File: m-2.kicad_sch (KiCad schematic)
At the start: 58 parts, among them J301 1-2199230-6, J302 2199230-6, M1 M2_4222, M301 M2_2280, U301 74LVC2G07GV, U302 74LVC2G07GV

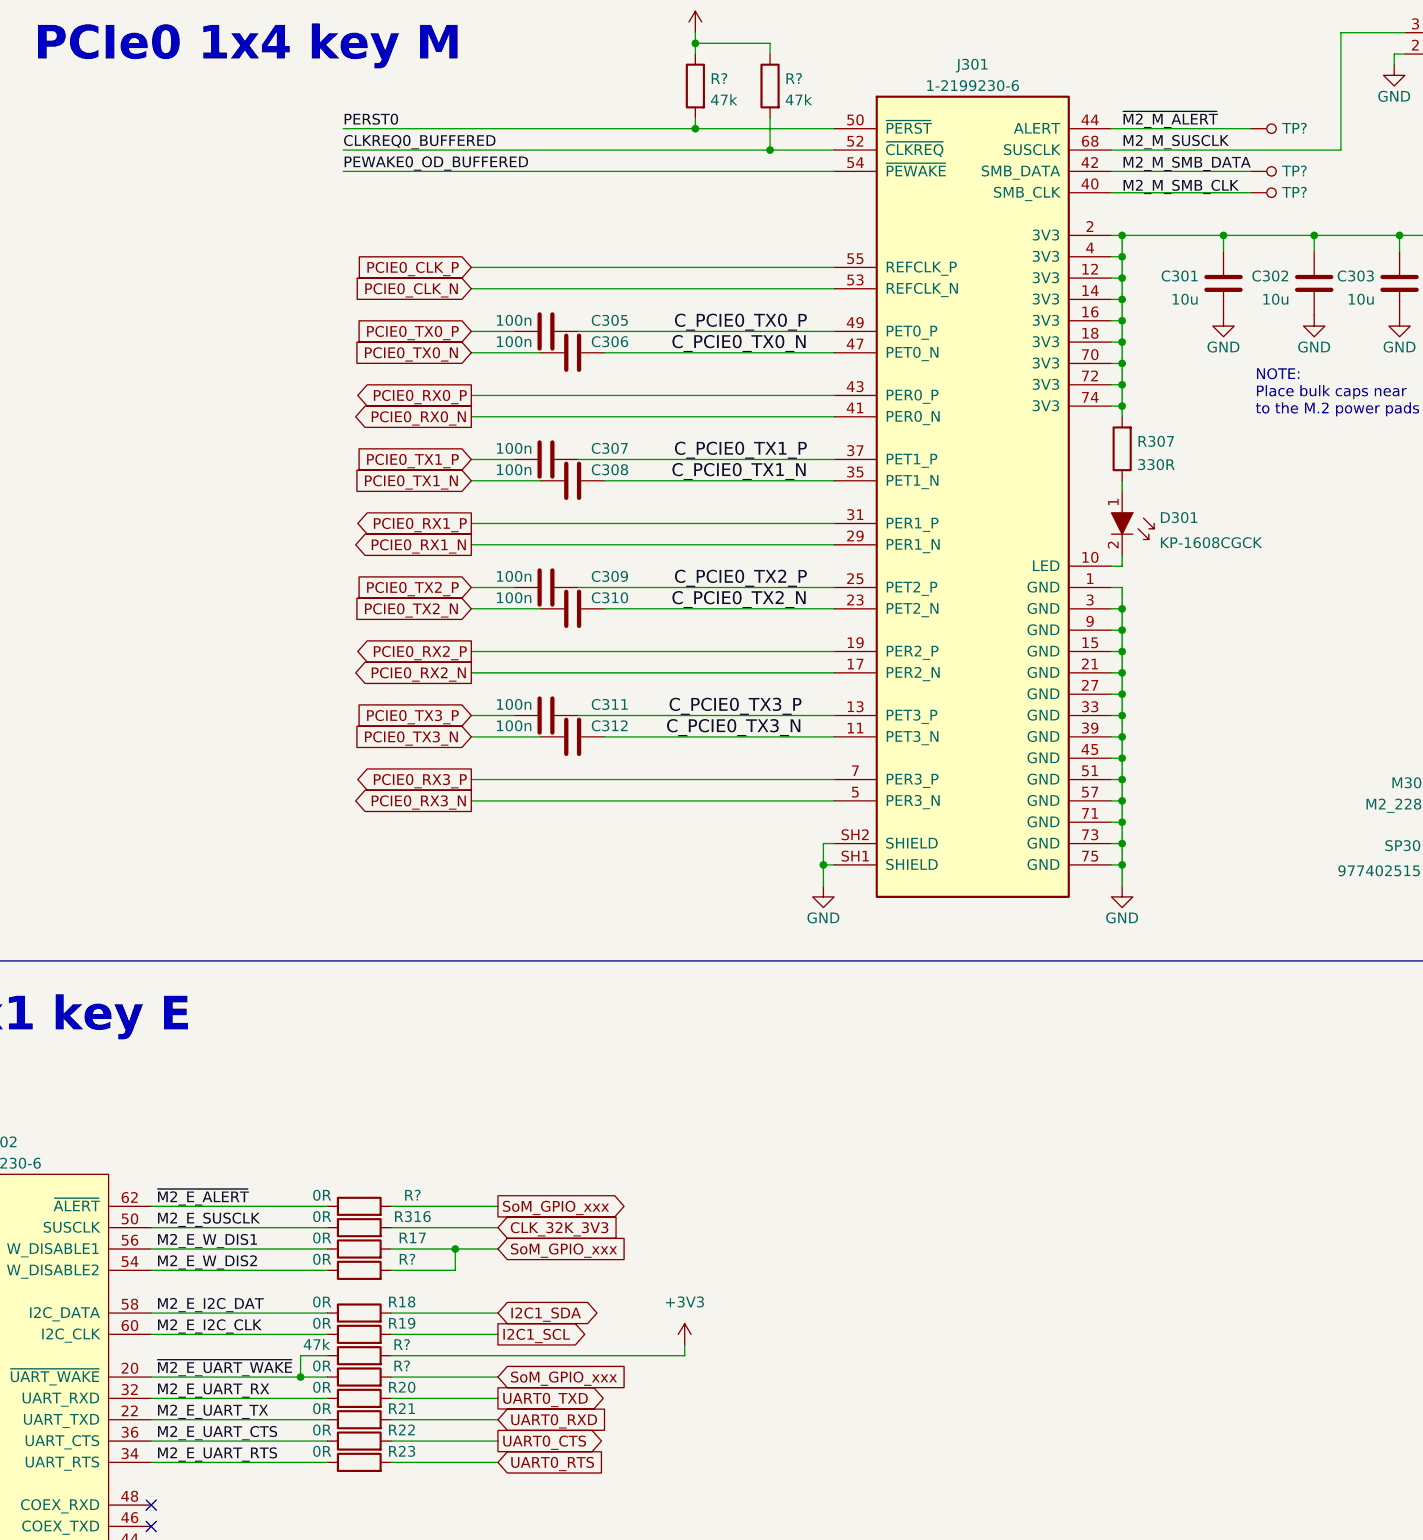
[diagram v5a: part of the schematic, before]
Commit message: Unused M.2 pins as test-point, M2 key E I2C and UART wake resistors set to DNP
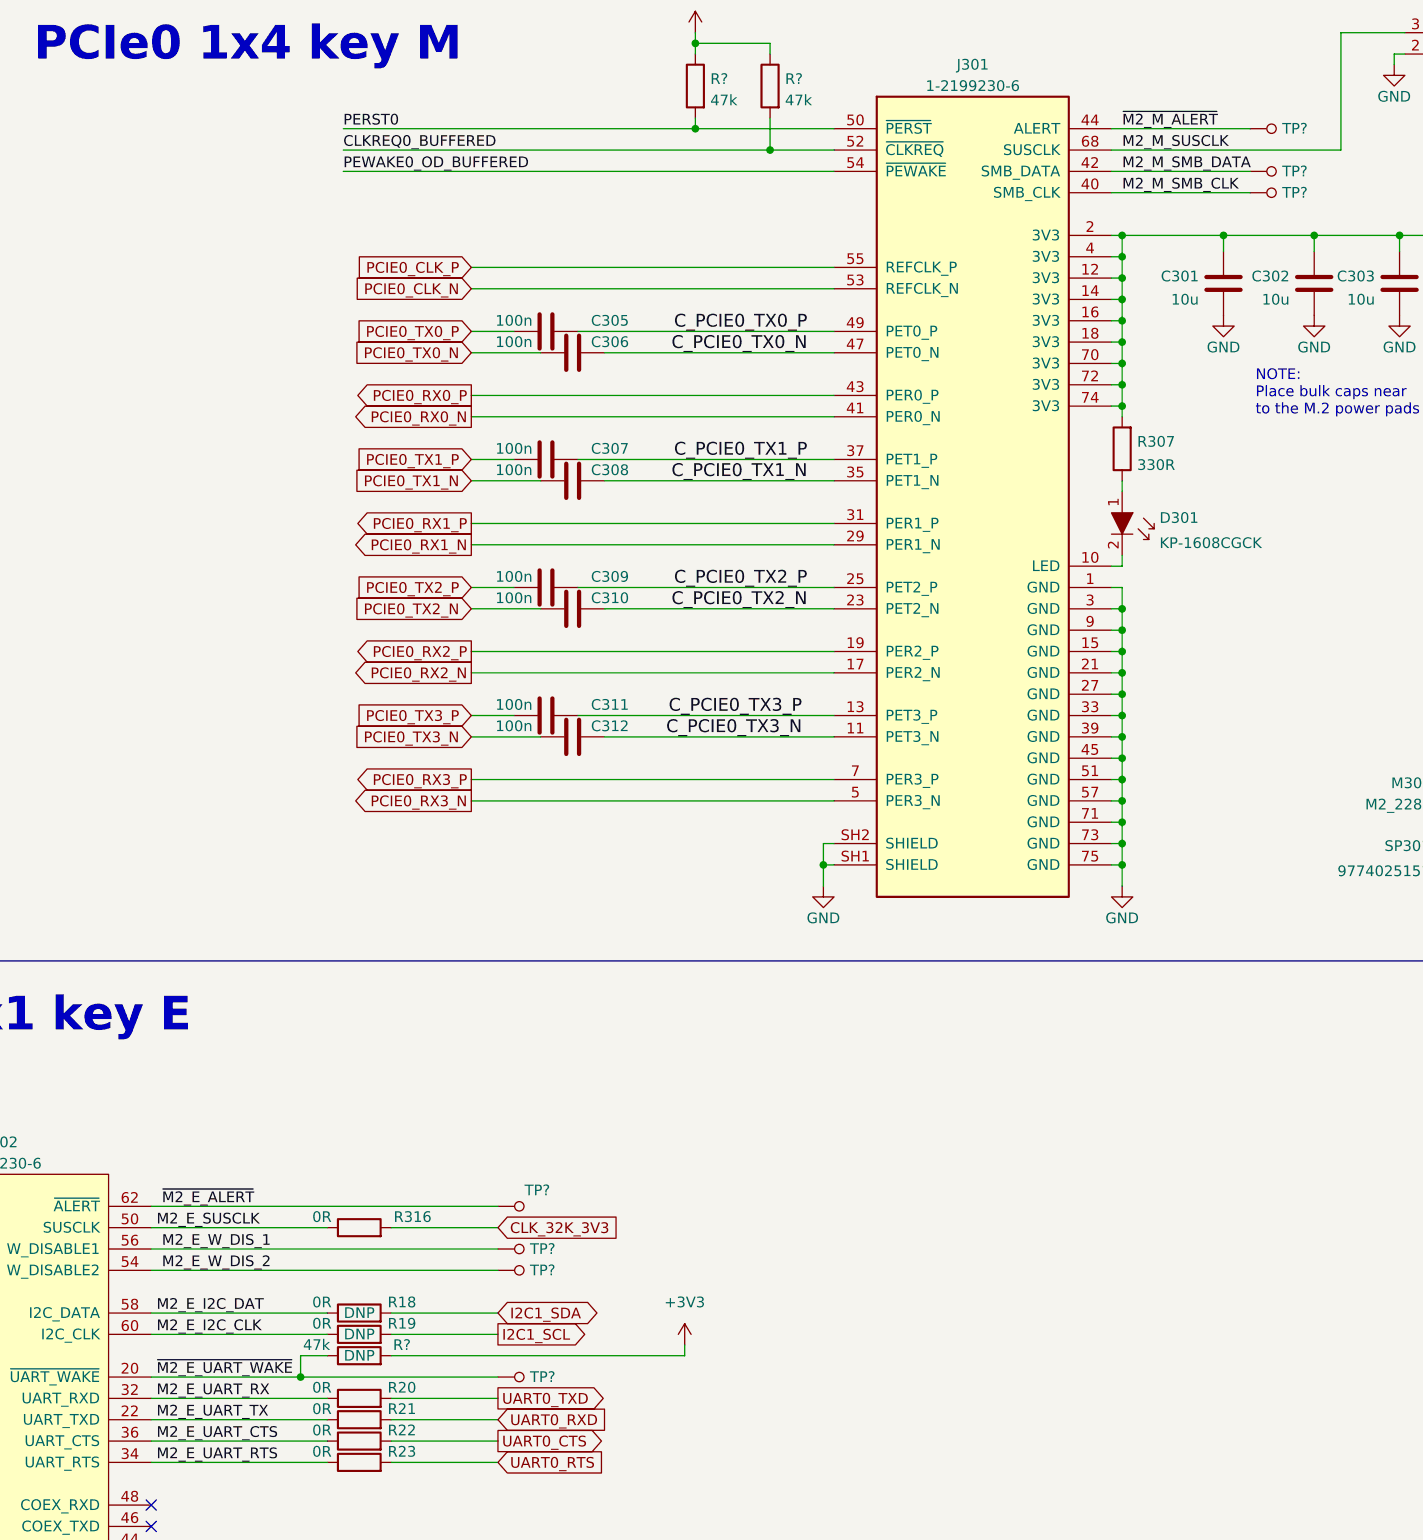
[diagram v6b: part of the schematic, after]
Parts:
- removed R17, R? (x3): R_0R_0402, antmicro-footprints:0402-res, symbol antmicroResistors0402:R_0R_0402
- added TP? (x4): TP_SMD_0_75MM, antmicro-footprints:Testpoint_smd_0_75mm, symbol antmicroTestPoints:TP_SMD_0_75MM
- R18, R19, R?: DNP (none) -> DNP
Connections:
- net M2_M_SMB_CLK: now also J301.40 (SMB_CLK), TP?.1
- net M2_M_SMB_DATA: now also J301.42 (SMB_DATA), TP?.1
- net ~{M2_E_ALERT}: now also TP?.1
- net ~{M2_E_UART_WAKE}: now also TP?.1
- net M2_E_W_DIS1 renamed M2_E_W_DIS_1
- net M2_E_W_DIS_1: now also TP?.1
- net M2_E_W_DIS2 renamed M2_E_W_DIS_2
- net M2_E_W_DIS_2: now also TP?.1

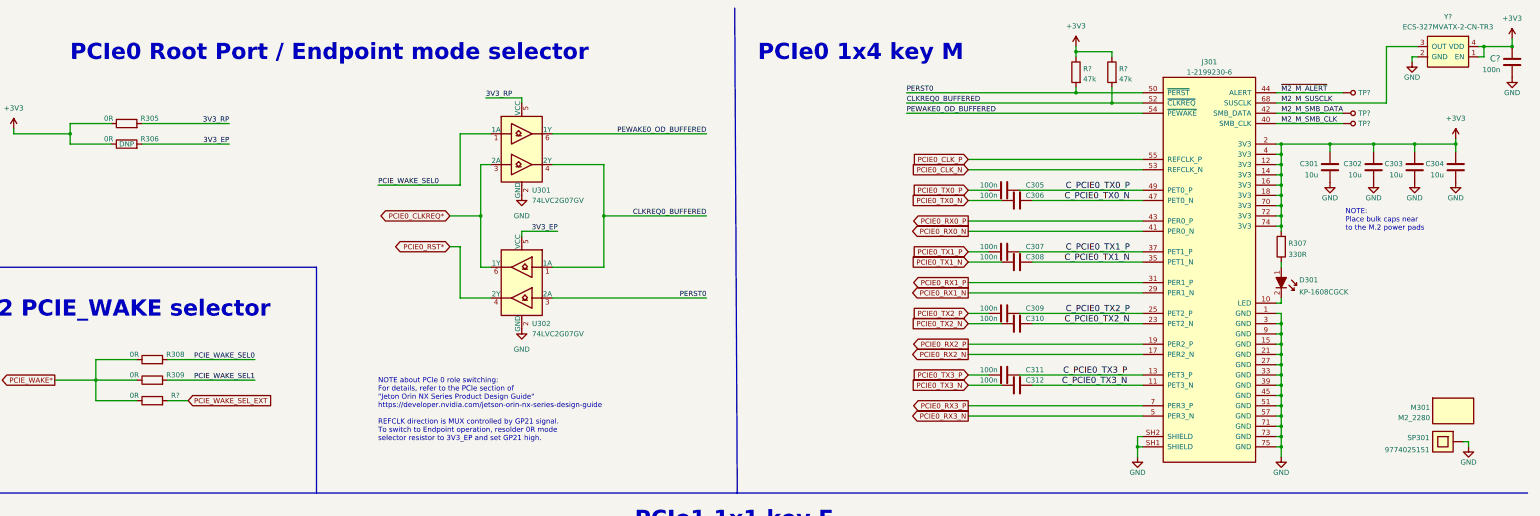
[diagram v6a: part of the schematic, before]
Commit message: Add R0 for PCIE0 ctrl signals
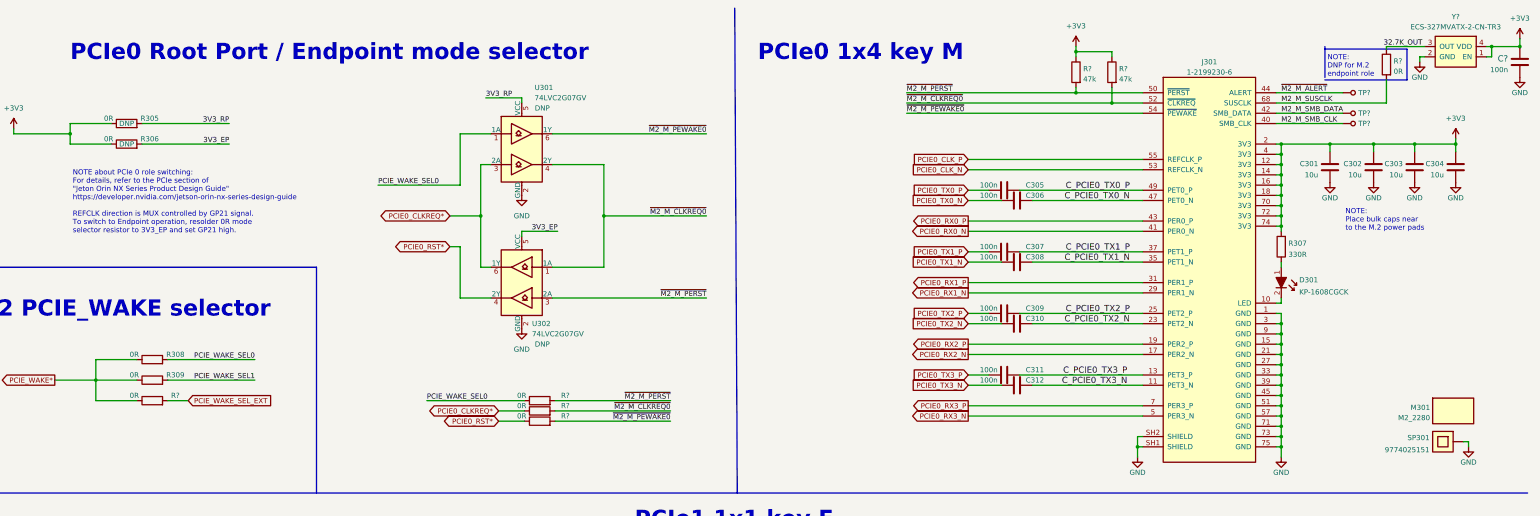
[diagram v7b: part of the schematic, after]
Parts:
- added R? (x4): R_0R_0402, antmicro-footprints:0402-res, symbol antmicroResistors0402:R_0R_0402
- R305, U301, U302: DNP (none) -> DNP
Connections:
- net M2_M_SUSCLK: now also R?.2; no longer Y?.3 (OUT)
- net PCIE0_CLKREQ*: now also R?.1
- net PCIE0_RST*: now also R?.1
- net PCIE_WAKE_SEL0: now also R?.1
- net CLKREQ0_BUFFERED renamed ~{M2_M_CLKREQ0}
- net ~{M2_M_CLKREQ0}: now also R?.2
- net PERST0 renamed ~{M2_M_PERST}
- net ~{M2_M_PERST}: now also R?.2
- net PEWAKE0_OD_BUFFERED renamed ~{M2_M_PEWAKE0}
- net ~{M2_M_PEWAKE0}: now also R?.2
- new net 32.7K_OUT: R?.1, Y?.3 (OUT)
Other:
- note added: "NOTE: DNP for M.2 endpoint role"
- moved on the sheet: C?, Y?

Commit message: Add decoupling to PCIe0 CTRL buffers, move all selection items closer
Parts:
- removed R305, R306, R?: R_0R_0402, antmicro-footprints:0402-res, symbol antmicroResistors0402:R_0R_0402
- added C? (x2): C_100n_0402, antmicro-footprints:0402-cap, symbol antmicroCapacitors0402:C_100n_0402
- added R?: R_0R_0402, antmicro-footprints:0402-res, symbol antmicroResistors0402:R_0R_0402
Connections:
- net 3V3_EP is gone; now on net +3V3: U302.5 (VCC)
- net 3V3_RP is gone; now on net +3V3: U301.5 (VCC)
- net +3V3: now also C?.1, C?.1
- net GND: now also C?.2, C?.2
- net M2_M_SUSCLK: now also R?.2
- net 32.7K_OUT renamed 32.7KHZ_OUT
- net 32.7KHZ_OUT: now also R?.1
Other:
- note added: "NOTE: DNP for M.2 key M endpoint role"
- note added: "NOTE: DNP for M.2 key M root port role"
- note removed: "NOTE: DNP for M.2 endpoint role"
- moved on the sheet: R?, U301, U302
